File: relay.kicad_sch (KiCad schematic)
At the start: 8 parts, among them J2 Conn_01x02_Pin, K1 SRD-05VDC-SL-C, Q1 S8050, U1 PC817X3NSZ1B

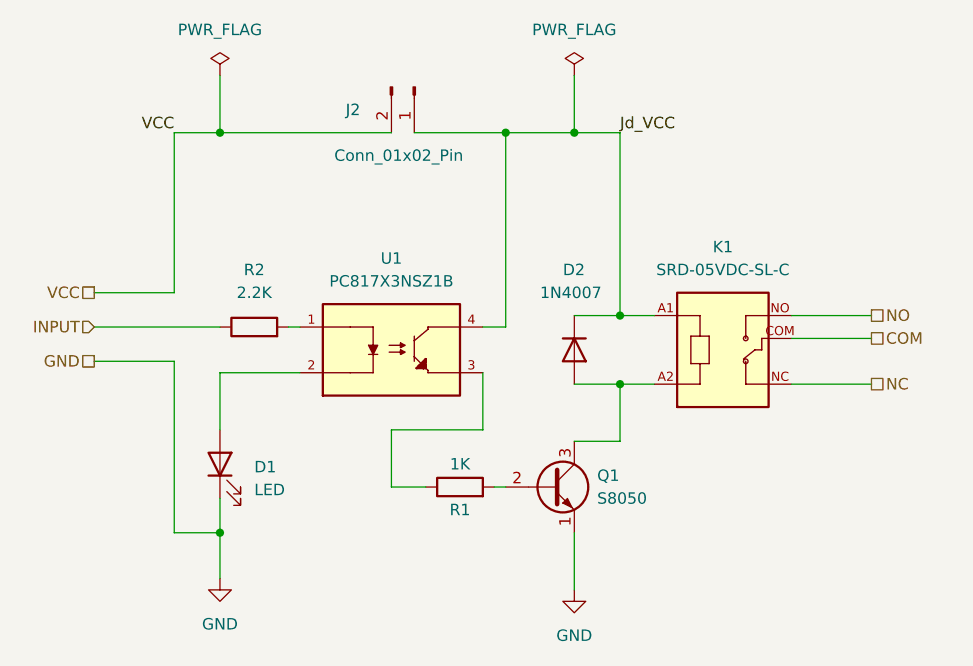
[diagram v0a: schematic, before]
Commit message: 30Amp Relay Schematic Completed
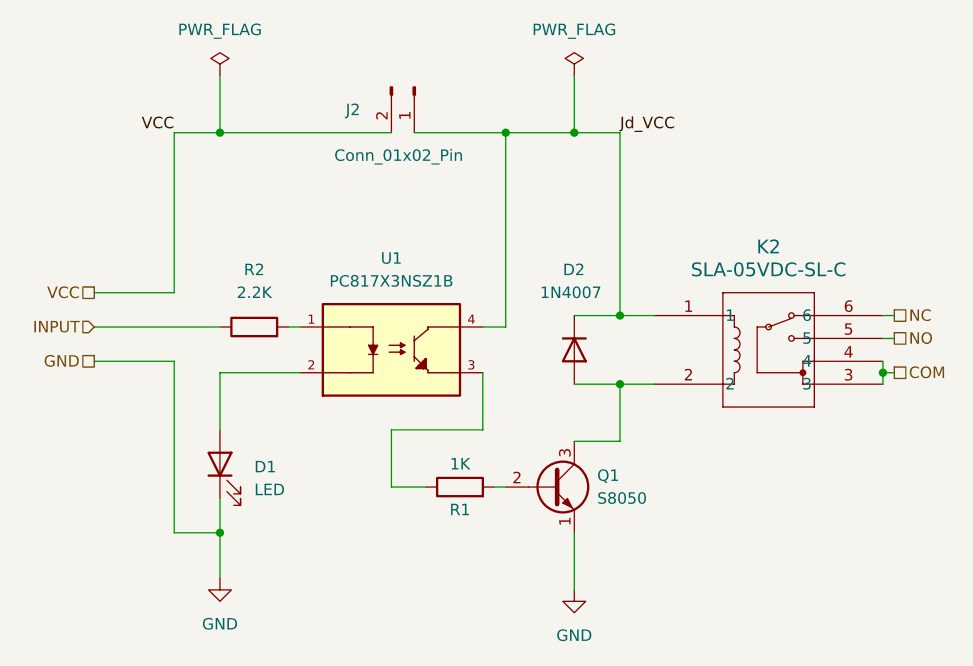
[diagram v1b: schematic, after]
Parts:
- removed K1: SRD-05VDC-SL-C, SRD-05VDC-SL-C:RELAY_SRD-05VDC-SL-C, symbol SRD-05VDC-SL-C:SRD-05VDC-SL-C
- added K2: SLA-05VDC-SL-C, K_SLA_C_NFR, symbol SLA-05VDC-SL-C:SLA-05VDC-SL-C
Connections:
- net COM: now also K2.3, K2.4
- net Jd_VCC: now also K2.1
- net NC: now also K2.6
- net NO: now also K2.5
- net at D2.2 (A), Q1.3 (C): now also K2.2
